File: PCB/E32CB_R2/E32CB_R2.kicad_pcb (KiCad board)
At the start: 2 copper layers, 111.3 x 90.9 mm, 89 parts, among them J1 GPIO_HEADER, J10 S, J11 Q4, J12 S, J13 Q3, J14 S, J15 Q8, J16 S, J17 Q7, J18 S, J19 Q6, J2 Power, J20 S, J21 Q5, J22 S, J3 USB_B, J4 USB +5V, J5 NEXTION, J6 I2C, J7 Q1, J8 S, J9 Q2, Q1 S8050, Q10 IRLR2905, Q2 S8050, Q3 IRLR2905, Q4 IRLR2905, Q5 IRLR2905, Q6 IRLR2905, Q7 IRLR2905, Q8 IRLR2905, Q9 IRLR2905, U1 ESP32-WROOM-32, X1 12MHz

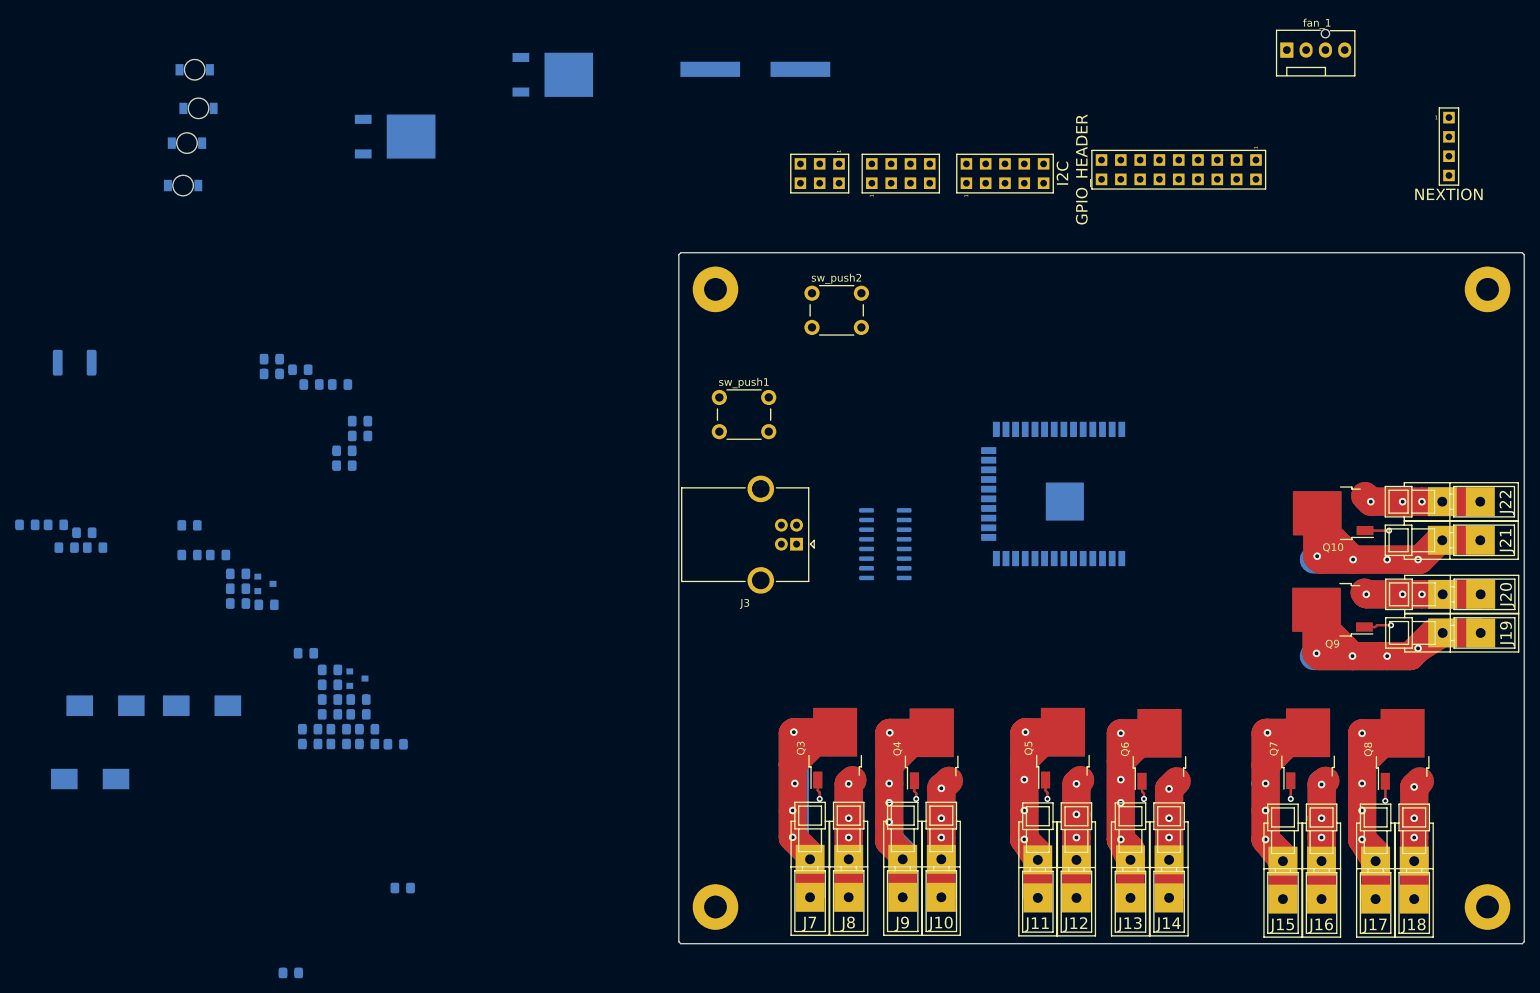
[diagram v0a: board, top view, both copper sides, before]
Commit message: reset section
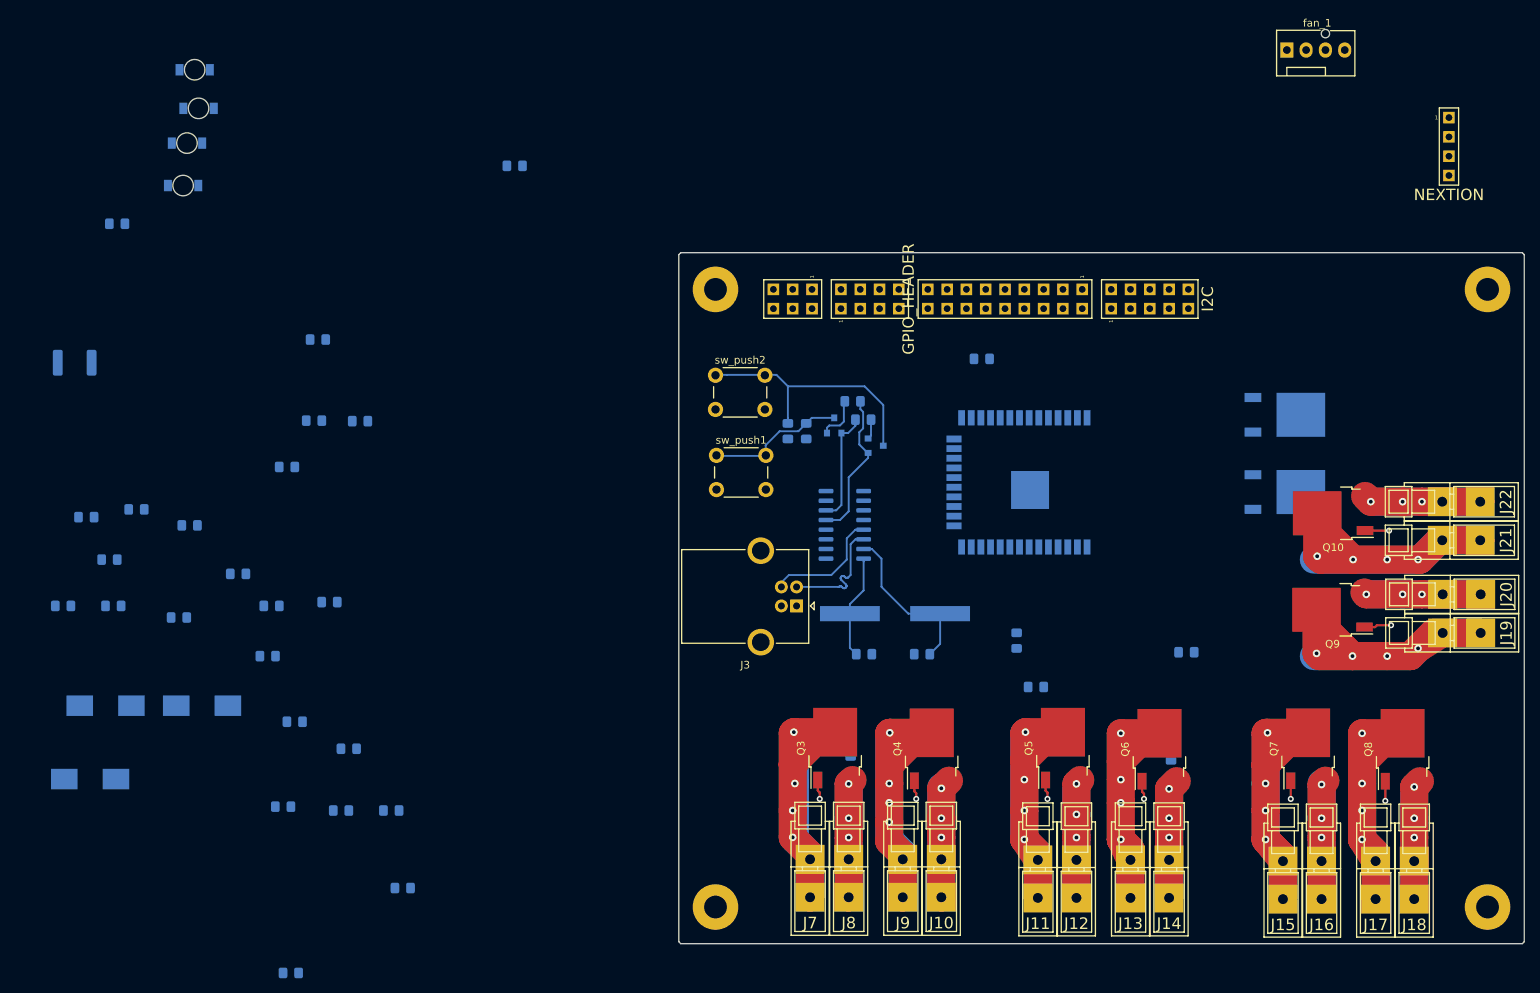
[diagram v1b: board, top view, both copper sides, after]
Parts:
- moved R25 132.9 mm to (181.4, 110.7), turned to 270 degrees
- moved 5Vstabilizer1 122.7 mm to (176.5, 67.3)
- moved R23 116.8 mm to (163.6, 98.6)
- moved R20 111.0 mm to (161.5, 111.8), turned to 270 degrees
- moved 3V3stabilizer1 110.9 mm to (176.5, 77.5)
- moved R6 97.7 mm to (136.6, 59.9)
- moved C1 93.2 mm to (128.8, 98.8), turned to 180 degrees
- moved C2 89.7 mm to (121.1, 98.8)
- moved R18 86.9 mm to (141.2, 97.0), turned to 90 degrees
- moved R14 84.6 mm to (143.8, 103.1)
- moved R9 83.4 mm to (119.6, 65.5)
- moved R10 82.2 mm to (121.0, 67.9), turned to 180 degrees
- moved Q1 77.7 mm to (117.2, 68.7), turned to 90 degrees
- moved R12 76.7 mm to (111.1, 69.5), turned to 90 degrees
- moved C8 76.6 mm to (75.2, 34.5)
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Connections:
- Q2 pad 3: /Boot -> /IO_0
- U1 pad 25: /Boot -> /IO_0
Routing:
- net /IO_0: track 0.00 -> 33.9 mm
- net Net-(C1-Pad1): track 0.00 -> 21.7 mm
- net Net-(CH340G1-Pad13): track 0.00 -> 19.9 mm
- net /EN: track 0.00 -> 18.4 mm
- net /USB_N: track 0.00 -> 15.9 mm
- net /USB_P: track 0.00 -> 15.9 mm
- net Net-(CH340G1-Pad14): track 0.00 -> 14.8 mm
- net Net-(C2-Pad1): track 0.00 -> 13.7 mm
- net Net-(Q1-Pad2): track 0.00 -> 5.97 mm
- net Net-(Q2-Pad2): track 0.00 -> 2.64 mm

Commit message: pcb update
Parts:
- removed sw_push1: RESET, Button_Switch_THT:SW_PUSH_6mm
- removed sw_push2: MODE, Button_Switch_THT:SW_PUSH_6mm
- added FLASH1: FLASH, Button_Switch_THT:SW_PUSH_6mm, F.Cu at (101.0, 58.4)
- added RESET1: RESET, Button_Switch_THT:SW_PUSH_6mm, F.Cu at (101.0, 69.8)
- moved J2 81.0 mm to (201.9, 64.8), turned to 180 degrees
- moved J4 62.2 mm to (174.0, 52.1)
- moved fan_1 43.1 mm to (191.8, 59.7), turned to 270 degrees
- moved J5 21.4 mm to (188.0, 50.8), turned to 90 degrees
- moved R14 8.36 mm to (135.9, 100.3)
- moved LED_R1 1.31 mm to (32.5, 38.0)
- moved J11 1.28 mm to (145.3, 128.5)
- moved J14 1.28 mm to (162.6, 128.5)
- moved Q5 1.28 mm to (148.6, 111.3)
- moved J12 1.28 mm to (150.4, 128.5)
- moved J13 1.28 mm to (157.5, 128.5)
- moved Q6 1.28 mm to (161.3, 111.4)
- moved R20 1.28 mm to (162.8, 111.9)
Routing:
- net /IO_0: track 33.9 -> 40.3 mm
- net /EN: track 18.4 -> 17.1 mm

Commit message: components on board
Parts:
- moved D3 177.9 mm to (189.5, 63.5), turned to 90 degrees
- moved R26 173.7 mm to (196.1, 111.8), turned to 270 degrees
- moved D2 167.8 mm to (184.4, 66.0), turned to 90 degrees
- moved R27 165.6 mm to (181.4, 90.4)
- moved D1 164.0 mm to (194.1, 69.6), turned to 270 degrees
- moved R28 161.9 mm to (183.5, 78.4)
- moved R24 161.8 mm to (183.9, 82.8)
- moved R22 153.2 mm to (190.5, 109.7), turned to 90 degrees
- moved R21 147.7 mm to (177.8, 107.7), turned to 90 degrees
- moved C7 128.6 mm to (167.8, 60.7)
- moved C9 121.8 mm to (164.6, 98.2), turned to 180 degrees
- moved C6 119.5 mm to (167.8, 57.5)
- moved C5 116.0 mm to (142.2, 61.0), turned to 180 degrees
- moved R19 108.9 mm to (150.9, 111.3), turned to 270 degrees
- moved C8 105.5 mm to (164.5, 90.7)
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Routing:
- net Net-(LED_R2-Pad2): track 0.00 -> 15.8 mm
- net Net-(LED_R1-Pad2): track 0.00 -> 10.1 mm
- net /IO_0: track 40.3 -> 32.4 mm
- net GND: track 0.00 -> 6.40 mm
- net +3V3: track 0.00 -> 6.39 mm
- net Net-(LED_R4-Pad2): track 0.00 -> 4.55 mm
- net Net-(LED_R3-Pad2): track 0.00 -> 3.77 mm

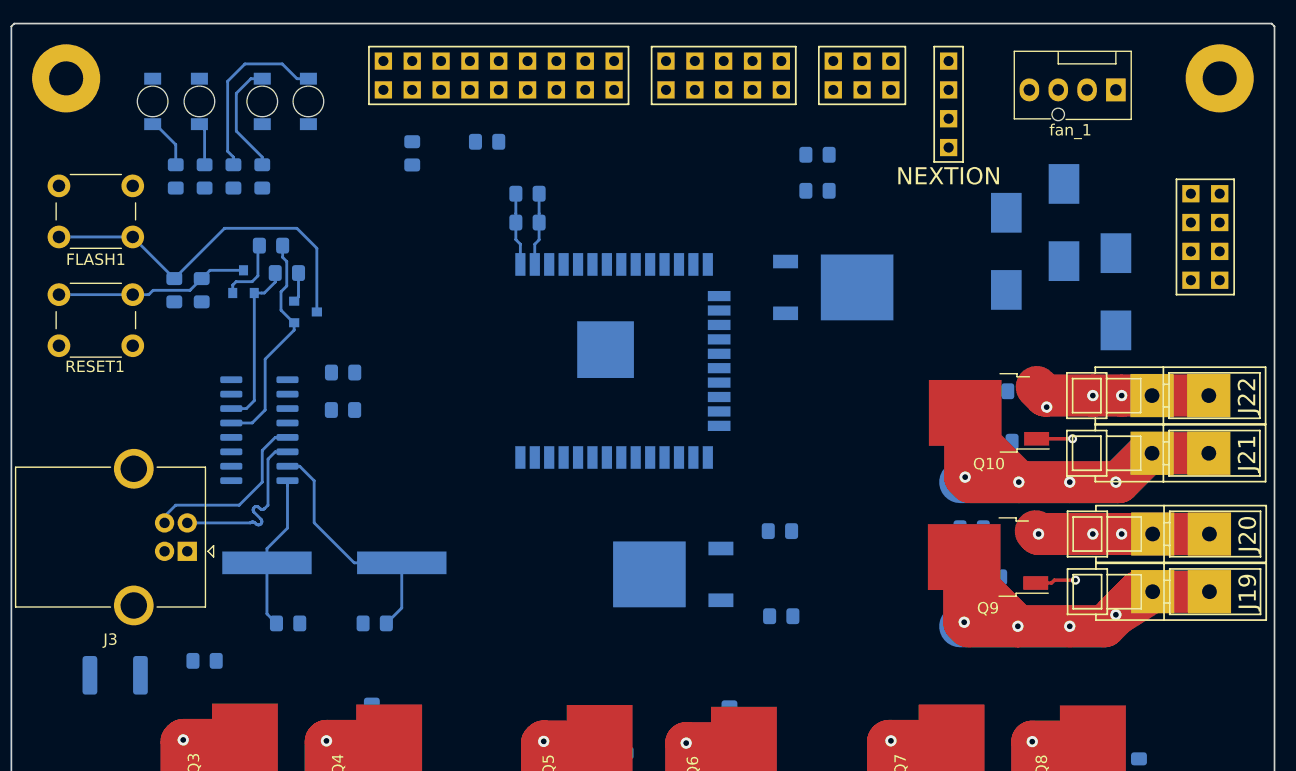
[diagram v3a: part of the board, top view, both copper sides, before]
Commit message: stabilizers position
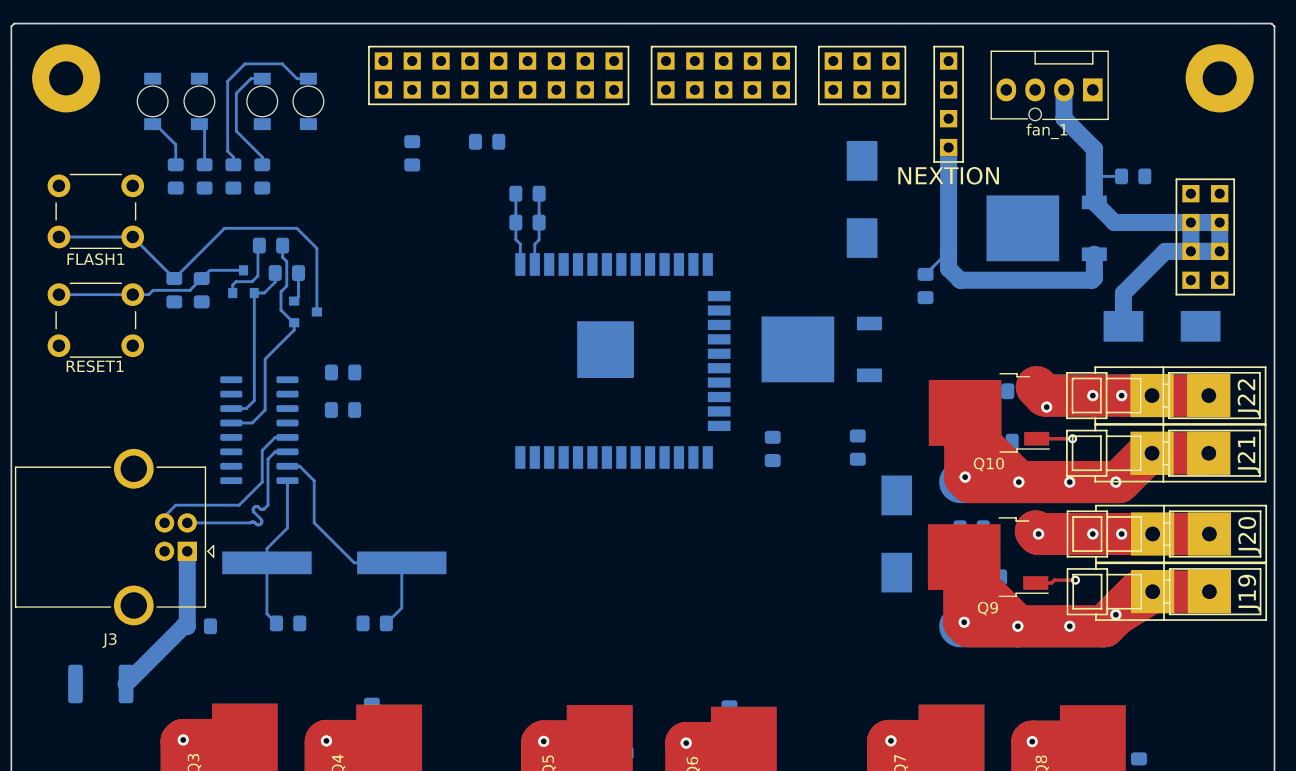
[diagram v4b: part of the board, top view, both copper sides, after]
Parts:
- moved D3 31.1 mm to (174.8, 90.9)
- moved C6 27.9 mm to (195.6, 59.4)
- moved 3V3stabilizer1 23.7 mm to (168.1, 74.7)
- moved 5Vstabilizer1 19.5 mm to (188.0, 64.0), turned to 180 degrees
- moved C9 16.3 mm to (171.3, 83.3), turned to 270 degrees
- moved D2 13.5 mm to (171.7, 61.5)
- moved C7 12.7 mm to (177.3, 69.1), turned to 270 degrees
- moved C8 7.27 mm to (163.8, 83.4), turned to 90 degrees
- moved D1 5.08 mm to (198.1, 72.6), turned to 0 degrees
- moved C3 3.09 mm to (113.3, 99.1)
- moved fan_1 2.03 mm to (192.0, 51.8)
- moved F1 1.48 mm to (104.6, 104.1)
- turned R24 to 180 degrees
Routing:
- net +12V: track 0.00 -> 45.7 mm
- net /display_Vin: track 0.00 -> 29.0 mm
- net Net-(C3-Pad1): track 0.00 -> 14.1 mm
